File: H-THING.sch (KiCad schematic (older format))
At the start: 19 parts, among them J1 MOTOR_CON, J2 PWR_PASSTHRU, J3 MAIN_PWR, J4 SIG_CON, Q1 2N3904, Q2 IRF5305, Q3 HUF75321, Q4 IRF5305, Q5 HUF75321, Q6 2N3904

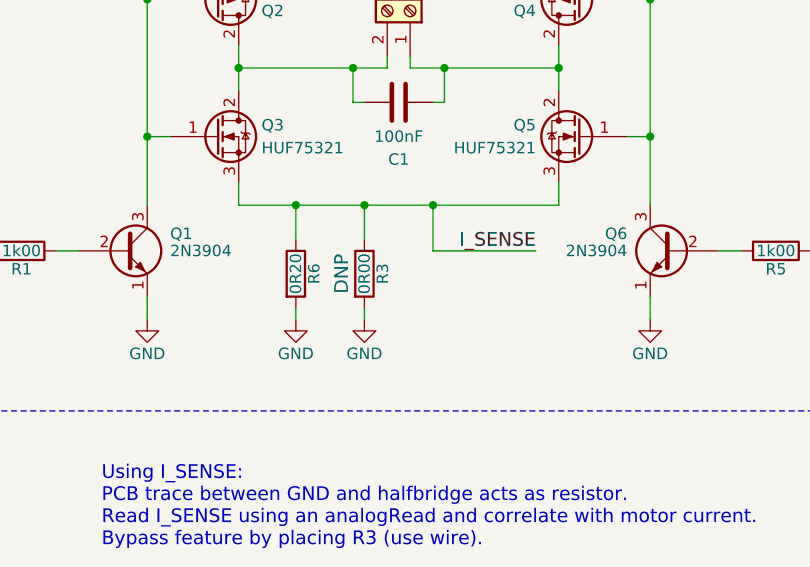
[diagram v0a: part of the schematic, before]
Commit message: Added images
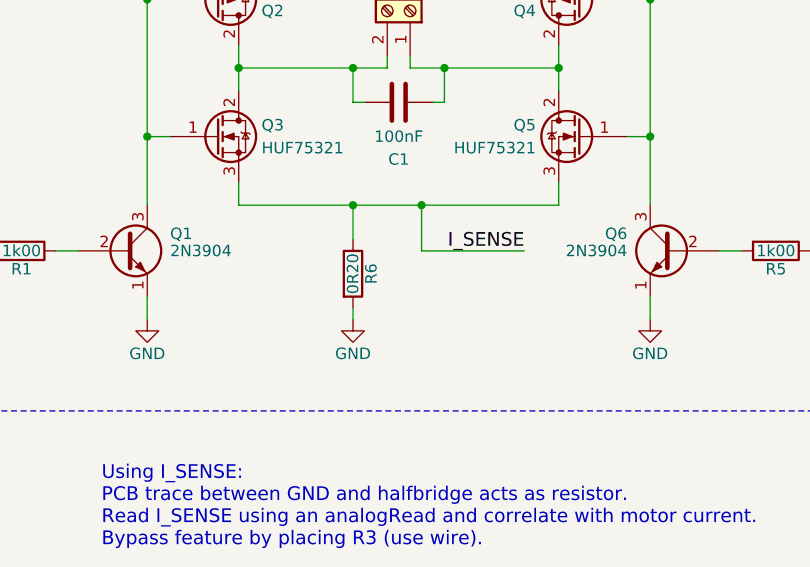
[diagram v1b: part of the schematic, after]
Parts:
- removed R3: 0R00, Resistors_THT:R_Axial_DIN0207_L6.3mm_D2.5mm_P2.54mm_Vertical, symbol R
- R6: footprint Resistors_THT:R_Axial_DIN0207_L6.3mm_D2.5mm_P10.16mm_Horizontal -> Resistors_THT:R_Axial_DIN0207_L6.3mm_D2.5mm_P2.54mm_Vertical
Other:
- moved on the sheet: R6
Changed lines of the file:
@@
 	3700 4450 3700 4550
-Wire Wire Line
-	3700 4550 5100 4550
 Wire Wire Line
 	5100 4550 5100 4450
@@
 L GND #PWR02
 U 1 1 5B19D9C4
-P 3950 5050
-F 0 "#PWR02" H 3950 4800 50  0001 C CNN
-F 1 "GND" H 3950 4900 50  0000 C CNN
-F 2 "" H 3950 5050 50  0001 C CNN
-F 3 "" H 3950 5050 50  0001 C CNN
-	1    3950 5050
-	1    0    0    -1
-$EndComp
-Connection ~ 3950 4550
+P 4200 5050
+F 0 "#PWR02" H 4200 4800 50  0001 C CNN
+F 1 "GND" H 4200 4900 50  0000 C CNN
+F 2 "" H 4200 5050 50  0001 C CNN
+F 3 "" H 4200 5050 50  0001 C CNN
+	1    4200 5050
+	1    0    0    -1
+$EndComp
+Connection ~ 4200 4550
 $Comp
 L VCC #PWR03
@@
 Text Notes 6950 4150 0    60   ~ 0
 Signal Connection
-Wire Wire Line
-	4250 4700 4250 4550
-Connection ~ 4250 4550
-$Comp
-L GND #PWR015
-U 1 1 5B1A066A
-P 4250 5050
-F 0 "#PWR015" H 4250 4800 50  0001 C CNN
-F 1 "GND" H 4250 4900 50  0000 C CNN
-F 2 "" H 4250 5050 50  0001 C CNN
-F 3 "" H 4250 5050 50  0001 C CNN
-	1    4250 5050
-	1    0    0    -1
-$EndComp
-Wire Wire Line
-	4250 5050 4250 5000
-Wire Wire Line
-	4550 4550 4550 4750
-Wire Wire Line
-	4550 4750 5000 4750
-Connection ~ 4550 4550
-Text Label 5000 4750 2    60   ~ 0
+Connection ~ 4500 4550
+Text Label 4950 4750 2    60   ~ 0
 I_SENSE
 Text Notes 3100 6050 0    60   ~ 0
 Using I_SENSE:\nPCB trace between GND and halfbridge acts as resistor.\nRead I_SENSE using an analogRead and correlate with motor current.\nBypass feature by placing R3 (use wire).
-$Comp
-L R R3
-U 1 1 5B1A060E
-P 4250 4850
-F 0 "R3" V 4330 4850 50  0000 C CNN
-F 1 "0R00" V 4250 4850 50  0000 C CNN
-F 2 "Resistors_THT:R_Axial_DIN0207_L6.3mm_D2.5mm_P2.54mm_Vertical" V 4180 4850 50  0001 C CNN
-F 3 "" H 4250 4850 50  0001 C CNN
-F 4 "DNP" V 4150 4850 60  0000 C CNN "DNP"
-	1    4250 4850
-	1    0    0    -1
-$EndComp
 $Comp
 L Conn_01x03_Female J4
@@
 L R R6
 U 1 1 5B1ABA86
-P 3950 4850
-F 0 "R6" V 4030 4850 50  0000 C CNN
-F 1 "0R20" V 3950 4850 50  0000 C CNN
-F 2 "Resistors_THT:R_Axial_DIN0207_L6.3mm_D2.5mm_P10.16mm_Horizontal" V 3880 4850 50  0001 C CNN
-F 3 "" H 3950 4850 50  0001 C CNN
-	1    3950 4850
-	1    0    0    -1
-$EndComp
-Wire Wire Line
-	3950 4700 3950 4550
-Wire Wire Line
-	3950 5050 3950 5000
+P 4200 4850
+F 0 "R6" V 4280 4850 50  0000 C CNN
+F 1 "0R20" V 4200 4850 50  0000 C CNN
+F 2 "Resistors_THT:R_Axial_DIN0207_L6.3mm_D2.5mm_P2.54mm_Vertical" V 4130 4850 50  0001 C CNN
+F 3 "" H 4200 4850 50  0001 C CNN
+	1    4200 4850
+	1    0    0    -1
+$EndComp
+Wire Wire Line
+	4200 4700 4200 4550
+Wire Wire Line
+	4200 5050 4200 5000
+Wire Wire Line
+	4500 4550 4500 4750
+Wire Wire Line
+	4500 4750 4950 4750
+Wire Wire Line
+	3700 4550 5100 4550
 $EndSCHEMATC

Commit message: Added FAB files
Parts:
- C1, C3: symbol C -> device:C
- C2: symbol CP -> device:CP
- J1, J2, J3: symbol Screw_Terminal_01x02 -> H-THING-rescue:Screw_Terminal_01x02
- J4: symbol Conn_01x03_Female -> H-THING-rescue:Conn_01x03_Female
- Q1, Q6: symbol 2N3904 -> H-THING-rescue:2N3904
- Q2, Q4: symbol Q_PMOS_GDS -> device:Q_PMOS_GDS
- Q3, Q5: symbol Q_NMOS_GDS -> device:Q_NMOS_GDS
- R1, R2, R4, R5, R6: symbol R -> device:R
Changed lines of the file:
@@
-EESchema Schematic File Version 2
-LIBS:power
-LIBS:device
-LIBS:switches
-LIBS:relays
-LIBS:motors
-LIBS:transistors
-LIBS:conn
-LIBS:linear
-LIBS:regul
-LIBS:74xx
-LIBS:cmos4000
-LIBS:adc-dac
-LIBS:memory
-LIBS:xilinx
-LIBS:microcontrollers
-LIBS:dsp
-LIBS:microchip
-LIBS:analog_switches
-LIBS:motorola
-LIBS:texas
-LIBS:intel
-LIBS:audio
-LIBS:interface
-LIBS:digital-audio
-LIBS:philips
-LIBS:display
-LIBS:cypress
-LIBS:siliconi
-LIBS:opto
-LIBS:atmel
-LIBS:contrib
-LIBS:valves
+EESchema Schematic File Version 4
 LIBS:H-THING-cache
-EELAYER 25 0
+EELAYER 26 0
 EELAYER END
 $Descr A4 11693 8268
@@
 $EndDescr
 $Comp
-L Q_NMOS_GDS Q3
+L device:Q_NMOS_GDS Q3
 U 1 1 5B19D5CC
 P 3600 4250
@@
 $EndComp
 $Comp
-L Q_PMOS_GDS Q2
+L device:Q_PMOS_GDS Q2
 U 1 1 5B19D62B
 P 3600 3650
@@
 $EndComp
 $Comp
-L Q_NMOS_GDS Q5
+L device:Q_NMOS_GDS Q5
 U 1 1 5B19D6B4
 P 5200 4250
@@
 $EndComp
 $Comp
-L Q_PMOS_GDS Q4
+L device:Q_PMOS_GDS Q4
 U 1 1 5B19D6BA
 P 5200 3650
@@
 $EndComp
 Wire Wire Line
-	3700 3850 3700 4050
-Wire Wire Line
-	5100 3850 5100 4050
+	3700 3850 3700 3950
+Wire Wire Line
+	5100 3850 5100 3950
 Wire Wire Line
 	3700 4450 3700 4550
@@
 	3700 3450 3700 3350
 Wire Wire Line
-	3700 3350 5100 3350
+	3700 3350 4400 3350
 Wire Wire Line
 	5100 3350 5100 3450
 $Comp
-L R R2
+L device:R R2
 U 1 1 5B19D715
 P 3300 3350
@@
 $EndComp
 $Comp
-L R R4
+L device:R R4
 U 1 1 5B19D78B
 P 5500 3350
@@
 	3400 3650 3300 3650
 Wire Wire Line
-	3300 3500 3300 4550
+	3300 3500 3300 3650
 Wire Wire Line
 	5400 3650 5500 3650
 Wire Wire Line
-	5500 3500 5500 4550
+	5500 3500 5500 3650
 Wire Wire Line
 	3300 4250 3400 4250
@@
 Connection ~ 5500 3650
 $Comp
-L 2N3904 Q1
+L H-THING-rescue:2N3904 Q1
 U 1 1 5B19D825
 P 3200 4750
@@
 $EndComp
 $Comp
-L 2N3904 Q6
+L H-THING-rescue:2N3904 Q6
 U 1 1 5B19D865
 P 5600 4750
@@
 Connection ~ 5500 4250
 $Comp
-L VCC #PWR01
+L power1:VCC #PWR01
 U 1 1 5B19D93A
 P 4400 3050
@@
 Connection ~ 4400 3350
 $Comp
-L GND #PWR02
+L power1:GND #PWR02
 U 1 1 5B19D9C4
 P 4200 5050
@@
 Connection ~ 4200 4550
 $Comp
-L VCC #PWR03
+L power1:VCC #PWR03
 U 1 1 5B19DA62
 P 3300 3050
@@
 $EndComp
 $Comp
-L VCC #PWR04
+L power1:VCC #PWR04
 U 1 1 5B19DABF
 P 5500 3050
@@
 	3300 3050 3300 3200
 $Comp
-L GND #PWR05
+L power1:GND #PWR05
 U 1 1 5B19DB8E
 P 3300 5050
@@
 $EndComp
 $Comp
-L GND #PWR06
+L power1:GND #PWR06
 U 1 1 5B19DBB1
 P 5500 5050
@@
 	3300 5050 3300 4950
 $Comp
-L R R1
+L device:R R1
 U 1 1 5B19DC29
 P 2750 4750
@@
 $EndComp
 $Comp
-L R R5
+L device:R R5
 U 1 1 5B19DC75
 P 6050 4750
@@
 HB2
 $Comp
-L Screw_Terminal_01x02 J1
+L H-THING-rescue:Screw_Terminal_01x02 J1
 U 1 1 5B19DEE0
 P 4450 3700
@@
 $EndComp
 Wire Wire Line
-	3700 3950 4350 3950
+	3700 3950 4200 3950
 Wire Wire Line
 	4350 3950 4350 3900
@@
 	4450 3900 4450 3950
 Wire Wire Line
-	4450 3950 5100 3950
+	4450 3950 4600 3950
 Connection ~ 5100 3950
 $Comp
-L C C1
+L device:C C1
 U 1 1 5B19E24C
 P 4400 4100
@@
 Connection ~ 4600 3950
 $Comp
-L Screw_Terminal_01x02 J3
+L H-THING-rescue:Screw_Terminal_01x02 J3
 U 1 1 5B19E758
 P 8100 3100
@@
 	8500 3200 8500 3350
 $Comp
-L VCC #PWR07
+L power1:VCC #PWR07
 U 1 1 5B19E8CE
 P 8500 2950
@@
 $EndComp
 $Comp
-L GND #PWR08
+L power1:GND #PWR08
 U 1 1 5B19E900
 P 8500 3350
@@
 $EndComp
 $Comp
-L CP C2
+L device:CP C2
 U 1 1 5B19EA69
 P 8950 3150
@@
 $EndComp
 $Comp
-L VCC #PWR09
+L power1:VCC #PWR09
 U 1 1 5B19EAE8
 P 8950 2950
@@
 $EndComp
 $Comp
-L GND #PWR010
+L power1:GND #PWR010
 U 1 1 5B19EB1D
 P 8950 3350
@@
 	8950 3350 8950 3300
 $Comp
-L C C3
+L device:C C3
 U 1 1 5B19ECF3
 P 9400 3150
@@
 $EndComp
 $Comp
-L VCC #PWR011
+L power1:VCC #PWR011
 U 1 1 5B19ED6F
 P 9400 2950
@@
 $EndComp
 $Comp
-L GND #PWR012
+L power1:GND #PWR012
 U 1 1 5B19EDA7
 P 9400 3350
@@
 	9400 3350 9400 3300
 $Comp
-L Screw_Terminal_01x02 J2
+L H-THING-rescue:Screw_Terminal_01x02 J2
 U 1 1 5B19F010
 P 7350 3200
@@
 	7750 3200 7750 3350
 $Comp
-L VCC #PWR013
+L power1:VCC #PWR013
 U 1 1 5B19F01A
 P 7750 2950
@@
 $EndComp
 $Comp
-L GND #PWR014
+L power1:GND #PWR014
 U 1 1 5B19F020
 P 7750 3350
@@
 Using I_SENSE:\nPCB trace between GND and halfbridge acts as resistor.\nRead I_SENSE using an analogRead and correlate with motor current.\nBypass feature by placing R3 (use wire).
 $Comp
-L Conn_01x03_Female J4
+L H-THING-rescue:Conn_01x03_Female J4
 U 1 1 5B1A0FE1
 P 8050 4850
@@
 Reverse connector to \nreverse motor direction
 $Comp
-L R R6
+L device:R R6
 U 1 1 5B1ABA86
 P 4200 4850
@@
 	4500 4750 4950 4750
 Wire Wire Line
-	3700 4550 5100 4550
+	3700 4550 4200 4550
+Wire Wire Line
+	3300 3650 3300 4250
+Wire Wire Line
+	5500 3650 5500 4250
+Wire Wire Line
+	3300 4250 3300 4550
+Wire Wire Line
+	5500 4250 5500 4550
+Wire Wire Line
+	4400 3350 5100 3350
+Wire Wire Line
+	4200 4550 4500 4550
+Wire Wire Line
+	3700 3950 3700 4050
+Wire Wire Line
+	5100 3950 5100 4050
+Wire Wire Line
+	4200 3950 4350 3950
+Wire Wire Line
+	4600 3950 5100 3950
+Wire Wire Line
+	4500 4550 5100 4550
 $EndSCHEMATC

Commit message: Updated 3d model with components
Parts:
- C1, C3: footprint Capacitors_THT:C_Disc_D5.0mm_W2.5mm_P5.00mm -> Capacitor_THT:C_Disc_D5.0mm_W2.5mm_P5.00mm
- C2: footprint Capacitors_THT:CP_Radial_D10.0mm_P5.00mm -> Capacitor_THT:CP_Radial_D10.0mm_P5.00mm
- J1, J2, J3: footprint Connectors_Terminal_Blocks:TerminalBlock_bornier-2_P5.08mm -> TerminalBlock:TerminalBlock_bornier-2_P5.08mm
- J4: footprint Socket_Strips:Socket_Strip_Straight_1x03_Pitch2.54mm -> Connector_PinSocket_2.54mm:PinSocket_1x03_P2.54mm_Vertical
- Q1, Q6: footprint TO_SOT_Packages_THT:TO-92_Inline_Narrow_Oval -> Package_TO_SOT_THT:TO-92_Inline
- Q2, Q3, Q4, Q5: footprint TO_SOT_Packages_THT:TO-220-3_Vertical -> Package_TO_SOT_THT:TO-220-3_Vertical
- R1, R2, R4, R5, R6: footprint Resistors_THT:R_Axial_DIN0207_L6.3mm_D2.5mm_P2.54mm_Vertical -> Resistor_THT:R_Axial_DIN0207_L6.3mm_D2.5mm_P2.54mm_Vertical
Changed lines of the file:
@@
 F 0 "Q3" H 3800 4300 50  0000 L CNN
 F 1 "HUF75321" H 3800 4200 50  0000 L CNN
-F 2 "TO_SOT_Packages_THT:TO-220-3_Vertical" H 3800 4350 50  0001 C CNN
+F 2 "Package_TO_SOT_THT:TO-220-3_Vertical" H 3800 4350 50  0001 C CNN
 F 3 "" H 3600 4250 50  0001 C CNN
 	1    3600 4250
@@
 F 0 "Q2" H 3800 3700 50  0000 L CNN
 F 1 "IRF5305" H 3800 3600 50  0000 L CNN
-F 2 "TO_SOT_Packages_THT:TO-220-3_Vertical" H 3800 3750 50  0001 C CNN
+F 2 "Package_TO_SOT_THT:TO-220-3_Vertical" H 3800 3750 50  0001 C CNN
 F 3 "" H 3600 3650 50  0001 C CNN
 	1    3600 3650
@@
 F 0 "Q5" H 5400 4300 50  0000 L CNN
 F 1 "HUF75321" H 5400 4200 50  0000 L CNN
-F 2 "TO_SOT_Packages_THT:TO-220-3_Vertical" H 5400 4350 50  0001 C CNN
+F 2 "Package_TO_SOT_THT:TO-220-3_Vertical" H 5400 4350 50  0001 C CNN
 F 3 "" H 5200 4250 50  0001 C CNN
 	1    5200 4250
@@
 F 0 "Q4" H 5400 3700 50  0000 L CNN
 F 1 "IRF5305" H 5400 3600 50  0000 L CNN
-F 2 "TO_SOT_Packages_THT:TO-220-3_Vertical" H 5400 3750 50  0001 C CNN
+F 2 "Package_TO_SOT_THT:TO-220-3_Vertical" H 5400 3750 50  0001 C CNN
 F 3 "" H 5200 3650 50  0001 C CNN
 	1    5200 3650
@@
 F 0 "R2" V 3380 3350 50  0000 C CNN
 F 1 "1k00" V 3300 3350 50  0000 C CNN
-F 2 "Resistors_THT:R_Axial_DIN0207_L6.3mm_D2.5mm_P2.54mm_Vertical" V 3230 3350 50  0001 C CNN
+F 2 "Resistor_THT:R_Axial_DIN0207_L6.3mm_D2.5mm_P2.54mm_Vertical" V 3230 3350 50  0001 C CNN
 F 3 "" H 3300 3350 50  0001 C CNN
 	1    3300 3350
@@
 F 0 "R4" V 5580 3350 50  0000 C CNN
 F 1 "1k00" V 5500 3350 50  0000 C CNN
-F 2 "Resistors_THT:R_Axial_DIN0207_L6.3mm_D2.5mm_P2.54mm_Vertical" V 5430 3350 50  0001 C CNN
+F 2 "Resistor_THT:R_Axial_DIN0207_L6.3mm_D2.5mm_P2.54mm_Vertical" V 5430 3350 50  0001 C CNN
 F 3 "" H 5500 3350 50  0001 C CNN
 	1    5500 3350
@@
 F 0 "Q1" H 3400 4825 50  0000 L CNN
 F 1 "2N3904" H 3400 4750 50  0000 L CNN
-F 2 "TO_SOT_Packages_THT:TO-92_Inline_Narrow_Oval" H 3400 4675 50  0001 L CIN
+F 2 "Package_TO_SOT_THT:TO-92_Inline" H 3400 4675 50  0001 L CIN
 F 3 "" H 3200 4750 50  0001 L CNN
 	1    3200 4750
@@
 F 0 "Q6" H 5800 4825 50  0000 L CNN
 F 1 "2N3904" H 5800 4750 50  0000 L CNN
-F 2 "TO_SOT_Packages_THT:TO-92_Inline_Narrow_Oval" H 5800 4675 50  0001 L CIN
+F 2 "Package_TO_SOT_THT:TO-92_Inline" H 5800 4675 50  0001 L CIN
 F 3 "" H 5600 4750 50  0001 L CNN
 	1    5600 4750
@@
 F 0 "R1" V 2830 4750 50  0000 C CNN
 F 1 "1k00" V 2750 4750 50  0000 C CNN
-F 2 "Resistors_THT:R_Axial_DIN0207_L6.3mm_D2.5mm_P2.54mm_Vertical" V 2680 4750 50  0001 C CNN
+F 2 "Resistor_THT:R_Axial_DIN0207_L6.3mm_D2.5mm_P2.54mm_Vertical" V 2680 4750 50  0001 C CNN
 F 3 "" H 2750 4750 50  0001 C CNN
 	1    2750 4750
@@
 F 0 "R5" V 6130 4750 50  0000 C CNN
 F 1 "1k00" V 6050 4750 50  0000 C CNN
-F 2 "Resistors_THT:R_Axial_DIN0207_L6.3mm_D2.5mm_P2.54mm_Vertical" V 5980 4750 50  0001 C CNN
+F 2 "Resistor_THT:R_Axial_DIN0207_L6.3mm_D2.5mm_P2.54mm_Vertical" V 5980 4750 50  0001 C CNN
 F 3 "" H 6050 4750 50  0001 C CNN
 	1    6050 4750
@@
 F 0 "J1" V 4650 3650 50  0000 C CNN
 F 1 "MOTOR_CON" V 4550 3650 50  0000 C CNN
-F 2 "Connectors_Terminal_Blocks:TerminalBlock_bornier-2_P5.08mm" H 4450 3700 50  0001 C CNN
+F 2 "TerminalBlock:TerminalBlock_bornier-2_P5.08mm" H 4450 3700 50  0001 C CNN
 F 3 "" H 4450 3700 50  0001 C CNN
 	1    4450 3700
@@
 F 0 "C1" V 4650 4100 50  0000 C CNN
 F 1 "100nF" V 4550 4100 50  0000 C CNN
-F 2 "Capacitors_THT:C_Disc_D5.0mm_W2.5mm_P5.00mm" H 4438 3950 50  0001 C CNN
+F 2 "Capacitor_THT:C_Disc_D5.0mm_W2.5mm_P5.00mm" H 4438 3950 50  0001 C CNN
 F 3 "" H 4400 4100 50  0001 C CNN
 	1    4400 4100
@@
 F 0 "J3" H 8100 3200 50  0000 C CNN
 F 1 "MAIN_PWR" H 8100 2900 50  0000 C CNN
-F 2 "Connectors_Terminal_Blocks:TerminalBlock_bornier-2_P5.08mm" H 8100 3100 50  0001 C CNN
+F 2 "TerminalBlock:TerminalBlock_bornier-2_P5.08mm" H 8100 3100 50  0001 C CNN
 F 3 "" H 8100 3100 50  0001 C CNN
 	1    8100 3100
@@
 F 0 "C2" H 8975 3250 50  0000 L CNN
 F 1 "470uF" H 8975 3050 50  0000 L CNN
-F 2 "Capacitors_THT:CP_Radial_D10.0mm_P5.00mm" H 8988 3000 50  0001 C CNN
+F 2 "Capacitor_THT:CP_Radial_D10.0mm_P5.00mm" H 8988 3000 50  0001 C CNN
 F 3 "" H 8950 3150 50  0001 C CNN
 	1    8950 3150
@@
 F 0 "C3" H 9425 3250 50  0000 L CNN
 F 1 "100nF" H 9425 3050 50  0000 L CNN
-F 2 "Capacitors_THT:C_Disc_D5.0mm_W2.5mm_P5.00mm" H 9438 3000 50  0001 C CNN
+F 2 "Capacitor_THT:C_Disc_D5.0mm_W2.5mm_P5.00mm" H 9438 3000 50  0001 C CNN
 F 3 "" H 9400 3150 50  0001 C CNN
 	1    9400 3150
@@
 F 0 "J2" H 7350 3300 50  0000 C CNN
 F 1 "PWR_PASSTHRU" H 7350 3000 50  0000 C CNN
-F 2 "Connectors_Terminal_Blocks:TerminalBlock_bornier-2_P5.08mm" H 7350 3200 50  0001 C CNN
+F 2 "TerminalBlock:TerminalBlock_bornier-2_P5.08mm" H 7350 3200 50  0001 C CNN
 F 3 "" H 7350 3200 50  0001 C CNN
 	1    7350 3200
@@
 F 0 "J4" H 8050 5050 50  0000 C CNN
 F 1 "SIG_CON" H 8050 4650 50  0000 C CNN
-F 2 "Socket_Strips:Socket_Strip_Straight_1x03_Pitch2.54mm" H 8050 4850 50  0001 C CNN
+F 2 "Connector_PinSocket_2.54mm:PinSocket_1x03_P2.54mm_Vertical" H 8050 4850 50  0001 C CNN
 F 3 "" H 8050 4850 50  0001 C CNN
 	1    8050 4850
@@
 F 0 "R6" V 4280 4850 50  0000 C CNN
 F 1 "0R20" V 4200 4850 50  0000 C CNN
-F 2 "Resistors_THT:R_Axial_DIN0207_L6.3mm_D2.5mm_P2.54mm_Vertical" V 4130 4850 50  0001 C CNN
+F 2 "Resistor_THT:R_Axial_DIN0207_L6.3mm_D2.5mm_P2.54mm_Vertical" V 4130 4850 50  0001 C CNN
 F 3 "" H 4200 4850 50  0001 C CNN
 	1    4200 4850
